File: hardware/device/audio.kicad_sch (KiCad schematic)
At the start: 42 parts, among them J5 AUDIO_EXP, J6 LINE_IN, J7 LINE_OUT, J9 HP_OUT, U24 WM8904CGEFL/RV, U28 TPS560200, U29 MAX98306xDT

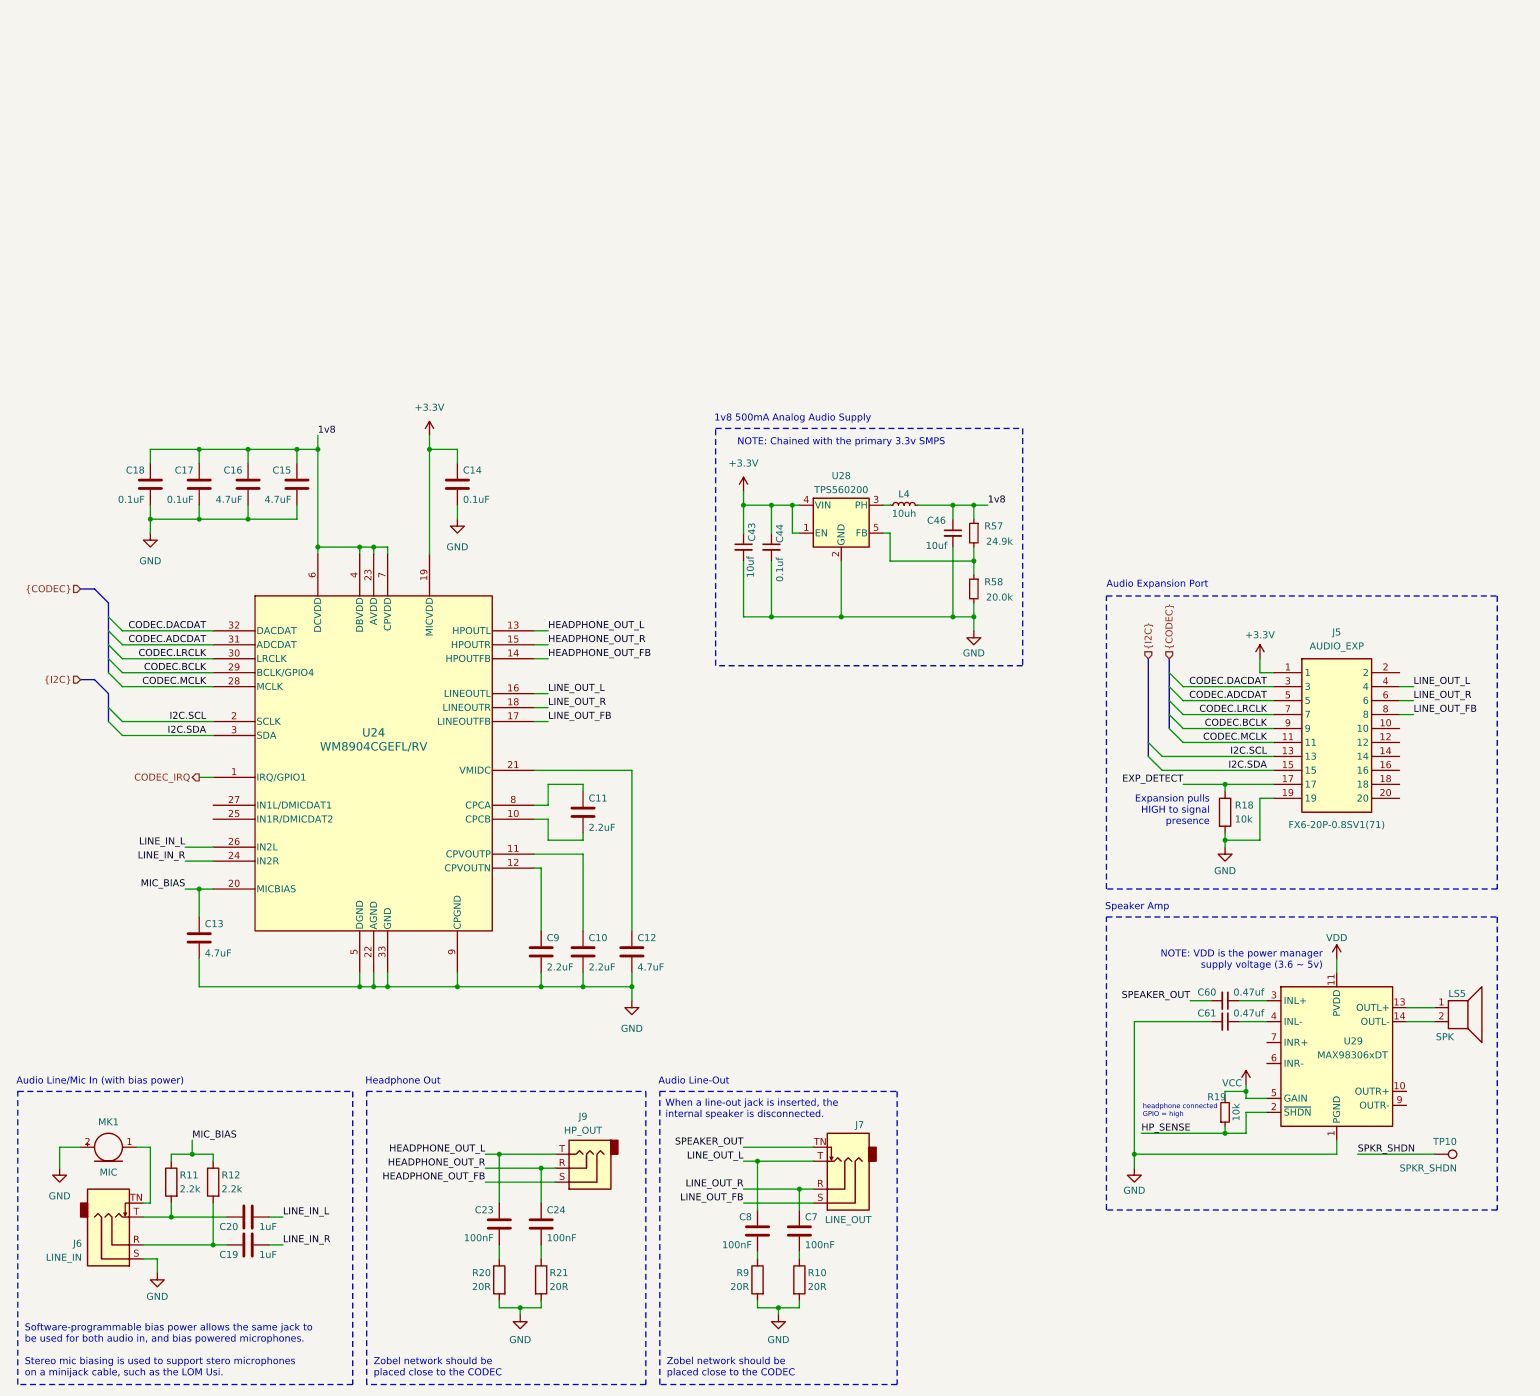
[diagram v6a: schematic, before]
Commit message: feat: change codec to NAU88C22YG
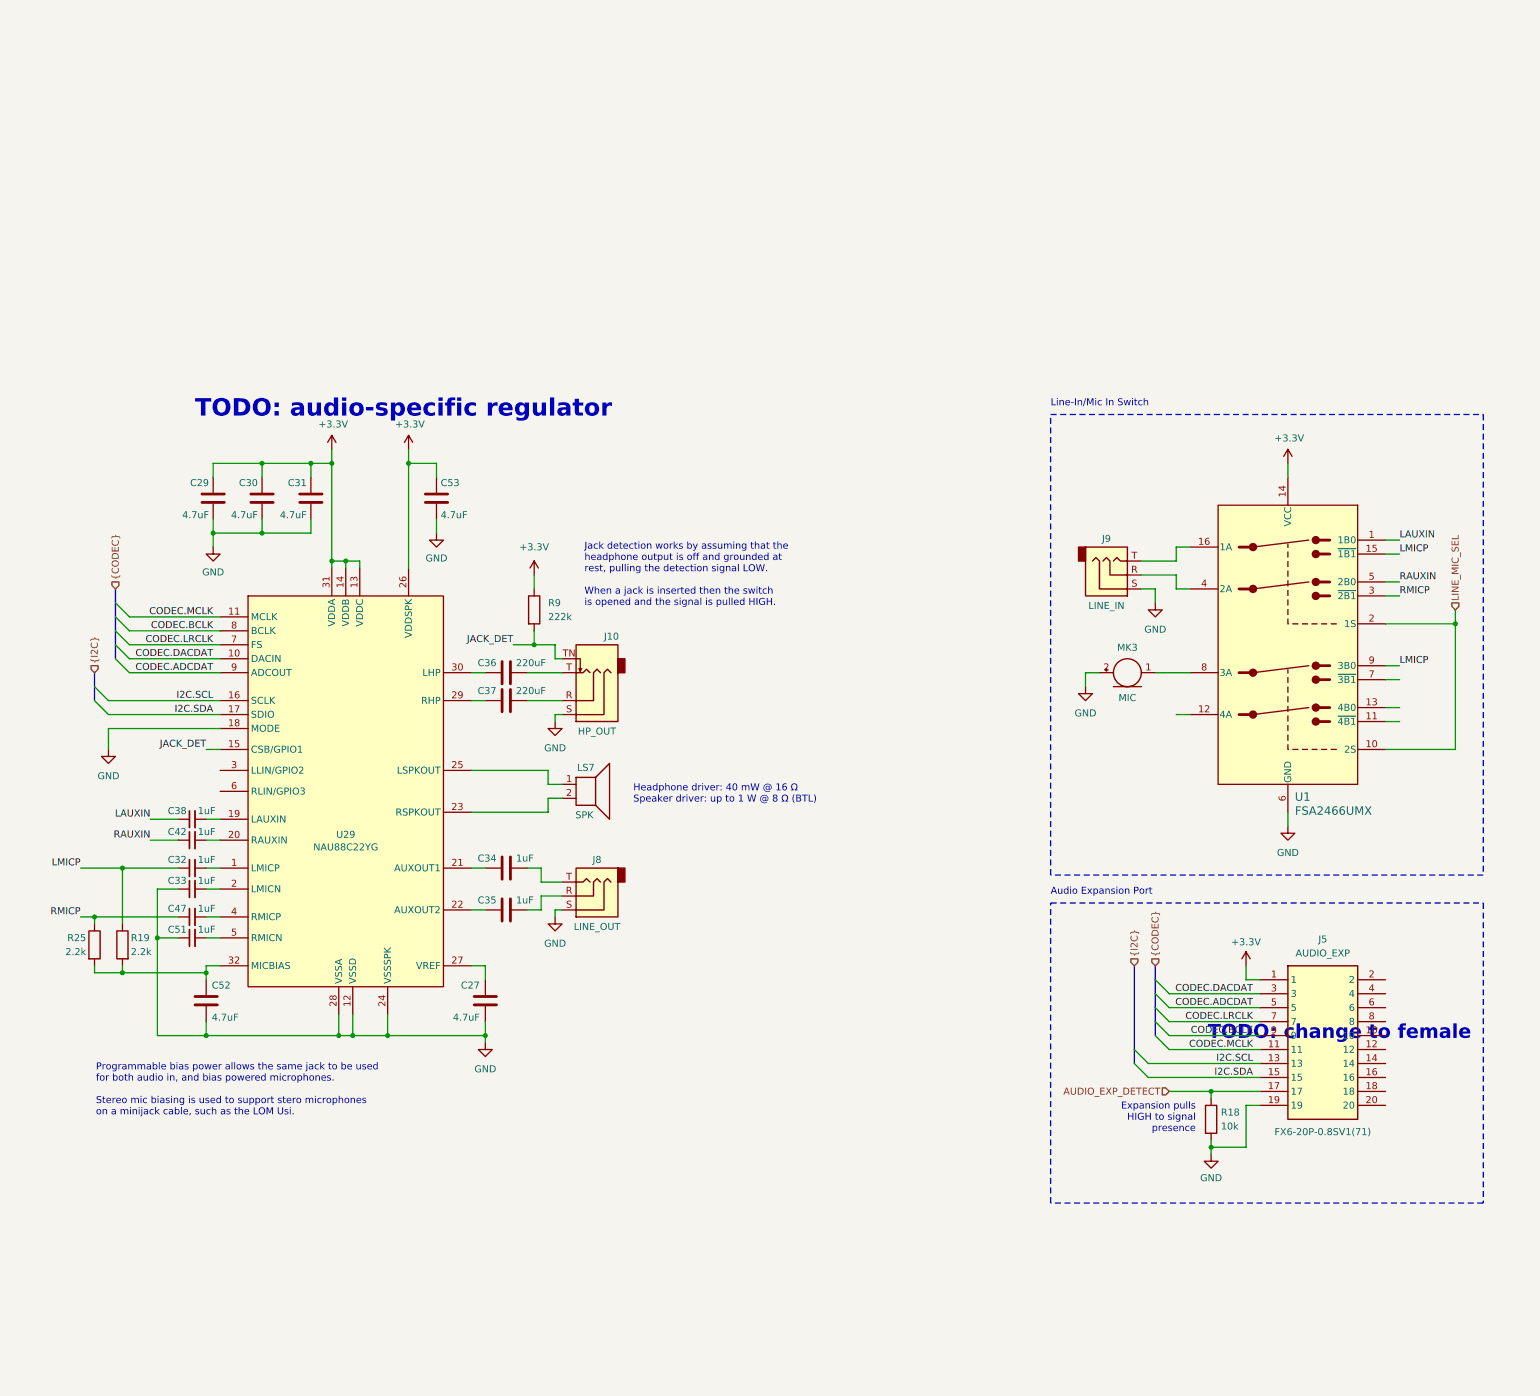
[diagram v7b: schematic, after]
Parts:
- removed C10, C11, C9: 2.2uF, Capacitor_SMD:C_0201_0603Metric, symbol Device:C
- removed C12, C13, C15, C16: 4.7uF, Capacitor_SMD:C_0201_0603Metric, symbol Device:C
- removed C14, C17, C18: 0.1uF, Capacitor_SMD:C_0201_0603Metric, symbol Device:C
- removed C19, C20: 1uF, Capacitor_SMD:C_0201_0603Metric, symbol Device:C
- removed C23, C24, C7, C8: 100nF, Capacitor_SMD:C_0201_0603Metric, symbol Device:C
- removed C43, C46: 10uf, Capacitor_SMD:C_0201_0603Metric, symbol Device:C_Small
- removed C44: 0.1uf, Capacitor_SMD:C_0201_0603Metric, symbol Device:C_Small
- removed C60, C61: 0.47uf, Capacitor_SMD:C_0201_0603Metric, symbol Device:C_Small
- removed J6: LINE_IN, Connector_Audio:Jack_3.5mm_CUI_SJ-3524-SMT_Horizontal, symbol Connector_Audio:AudioJack3_SwitchT
- removed J7: LINE_OUT, Connector_Audio:Jack_3.5mm_CUI_SJ-3524-SMT_Horizontal, symbol Connector_Audio:AudioJack3_SwitchT
- removed L4: 10uh, symbol Device:L_Small
- removed LS5: SPK, symbol Device:Speaker
- removed MK1: MIC, symbol Device:Microphone
- removed R10, R20, R21: 20R, Resistor_SMD:R_0201_0603Metric, symbol Device:R
- removed R11, R12: 2.2k, Resistor_SMD:R_0201_0603Metric, symbol Device:R
- removed R19: 10k, Resistor_SMD:R_0201_0603Metric, symbol Device:R_Small
- removed R57: 24.9k, Resistor_SMD:R_0201_0603Metric, symbol Device:R_Small
- removed R58: 20.0k, Resistor_SMD:R_0201_0603Metric, symbol Device:R_Small
- removed TP10: SPKR_SHDN, TestPoint:TestPoint_Pad_D2.5mm, symbol Connector:TestPoint
- removed U24: WM8904CGEFL/RV, pocket_synth:WM8904CGEFL_RV, symbol pocket_synth:WM8904CGEFL_RV
- removed U28: TPS560200, Package_TO_SOT_SMD:SOT-23-5, symbol Regulator_Switching:TPS560200
- removed U29: MAX98306xDT, Package_DFN_QFN:TDFN-14-1EP_3x3mm_P0.4mm_EP1.78x2.35mm, symbol Amplifier_Audio:MAX98306xDT
- added C27, C29, C30, C31, C52, C53: 4.7uF, Capacitor_SMD:C_0201_0603Metric, symbol Device:C
- added C32, C33, C38, C42, C47, C51: 1uF, Capacitor_SMD:C_0201_0603Metric, symbol Device:C_Small
- added C34, C35: 1uF, Capacitor_SMD:C_0201_0603Metric, symbol Device:C
- added C36, C37: 220uF, Capacitor_SMD:C_0201_0603Metric, symbol Device:C
- added J10: HP_OUT, Connector_Audio:Jack_3.5mm_CUI_SJ-3524-SMT_Horizontal, symbol Connector_Audio:AudioJack3_SwitchT
- added J8: LINE_OUT, Connector_Audio:Jack_3.5mm_CUI_SJ-3523-SMT_Horizontal, symbol Connector_Audio:AudioJack3
- added LS7: SPK, symbol Device:Speaker
- added MK3: MIC, symbol Device:Microphone
- added R19, R25: 2.2k, Resistor_SMD:R_0201_0603Metric, symbol Device:R
- added U1: FSA2466UMX, pocket_synth:FSA2466UMX, symbol pocket_synth:FSA2466UMX
- added U29: NAU88C22YG, pocket_synth:NAU88C22YG, symbol pocket_synth:NAU88C22YG
- J9: value HP_OUT -> LINE_IN
- R9: value 20R -> 222k
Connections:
- net HEADPHONE_OUT_FB is gone; now on net GND: J9.S
- net +3.3V: now also R9.1, C29.1, C30.1, C31.1, C53.1, U1.14 (VCC), U29.13 (VDDC), U29.14 (VDDB), U29.26 (VDDSPK), U29.31 (VDDA)
- net CODEC.ADCDAT: now also U29.9 (ADCOUT)
- net CODEC.BCLK: now also U29.8 (BCLK)
- net CODEC.DACDAT: now also U29.10 (DACIN)
- net CODEC.LRCLK: now also U29.7 (FS)
- net CODEC.MCLK: now also U29.11 (MCLK)
- net GND: now also C27.2, C29.2, C30.2, C31.2, C33.1, C51.1, C52.2, C53.2, J10.S, J8.S, MK3.2 (+), U1.6 (GND), U29.12 (VSSD), U29.18 (MODE), U29.24 (VSSSPK), U29.28 (VSSA); no longer R9.2
- net I2C.SCL: now also U29.16 (SCLK)
- net I2C.SDA: now also U29.17 (SDIO)
- net EXP_DETECT renamed AUDIO_EXP_DETECT
- net HEADPHONE_OUT_L: no longer names the net of J9.T
- net HEADPHONE_OUT_L: now also U1.16 (1A)
- net HEADPHONE_OUT_R: no longer names the net of J9.R
- net HEADPHONE_OUT_R: now also U1.4 (2A)
- net LINE_OUT_FB: no longer names the net of J5.8
- net LINE_OUT_L: no longer names the net of J5.4
- net LINE_OUT_R: no longer names the net of J5.6
- new net: C35.2, J8.R
- new net: C34.2, J8.T
- new net: C38.2, U29.19 (LAUXIN)
- new net: C52.1, R19.2, R25.2, U29.32 (MICBIAS)
- new net: C32.2, U29.1 (LMICP)
- new net: C33.2, U29.2 (LMICN)
- new net: C42.2, U29.20 (RAUXIN)
- new net: C34.1, U29.21 (AUXOUT1)
- new net: C35.1, U29.22 (AUXOUT2)
- new net: LS7.2, U29.23 (RSPKOUT)
- new net: LS7.1, U29.25 (LSPKOUT)
- new net: C27.1, U29.27 (VREF)
- new net: C37.1, U29.29 (RHP)
- new net: C36.1, U29.30 (LHP)
- new net: C47.2, U29.4 (RMICP)
- new net: C51.2, U29.5 (RMICN)
- new net: C37.2, J10.R
- new net: C36.2, J10.T
- new net: MK3.1 (-), U1.8 (3A)
- new net JACK_DET: J10.TN, R9.2, U29.15 (CSB/GPIO1)
- new net LAUXIN: C38.1, U1.1 (1B0)
- new net LINE_MIC_SEL: U1.10 (2S), U1.2 (1S)
- new net LMICP: C32.1, R19.1, U1.15 (~{1B1}), U1.9 (3B0)
- new net RAUXIN: C42.1, U1.5 (2B0)
- new net RMICP: C47.1, R25.1, U1.3 (~{2B1})
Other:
- note added: "Headphone driver: 40 mW @ 16 Ω Speaker driver: up to 1 W @ 8 Ω (BTL)"
- note added: "Jack detection works by assuming that the headphone output is off and grounded at rest, pulling the detection signal LOW. When a jack is inserted then the switch is opened and the signal is pulled HIGH."
- note added: "Line-In/Mic In Switch"
- note added: "Programmable bias power allows the same jack to be used for both audio in, and bias powered microphones. Stereo mic biasing is used to support stero microphones on a minijack cable, such as the LOM Usi."
- note added: "TODO: audio-specific regulator"
- note added: "TODO: change to female"
- note removed: "1v8 500mA Analog Audio Supply"
- note removed: "Audio Line-Out"
- note removed: "Audio Line/Mic In (with bias power)"
- note removed: "Headphone Out"
- note removed: "NOTE: Chained with the primary 3.3v SMPS"
- note removed: "NOTE: VDD is the power manager supply voltage (3.6 ~ 5v)"
- note removed: "Software-programmable bias power allows the same jack to be used for both audio in, and bias powered microphones. Stereo mic biasing is used to support stero microphones on a minijack cable, such as the LOM Usi."
- note removed: "Speaker Amp"
- note removed: "When a line-out jack is inserted, the internal speaker is disconnected."
- note removed: "Zobel network should be placed close to the CODEC"
- note removed: "headphone connected GPIO = high"
- moved on the sheet: J5, R18

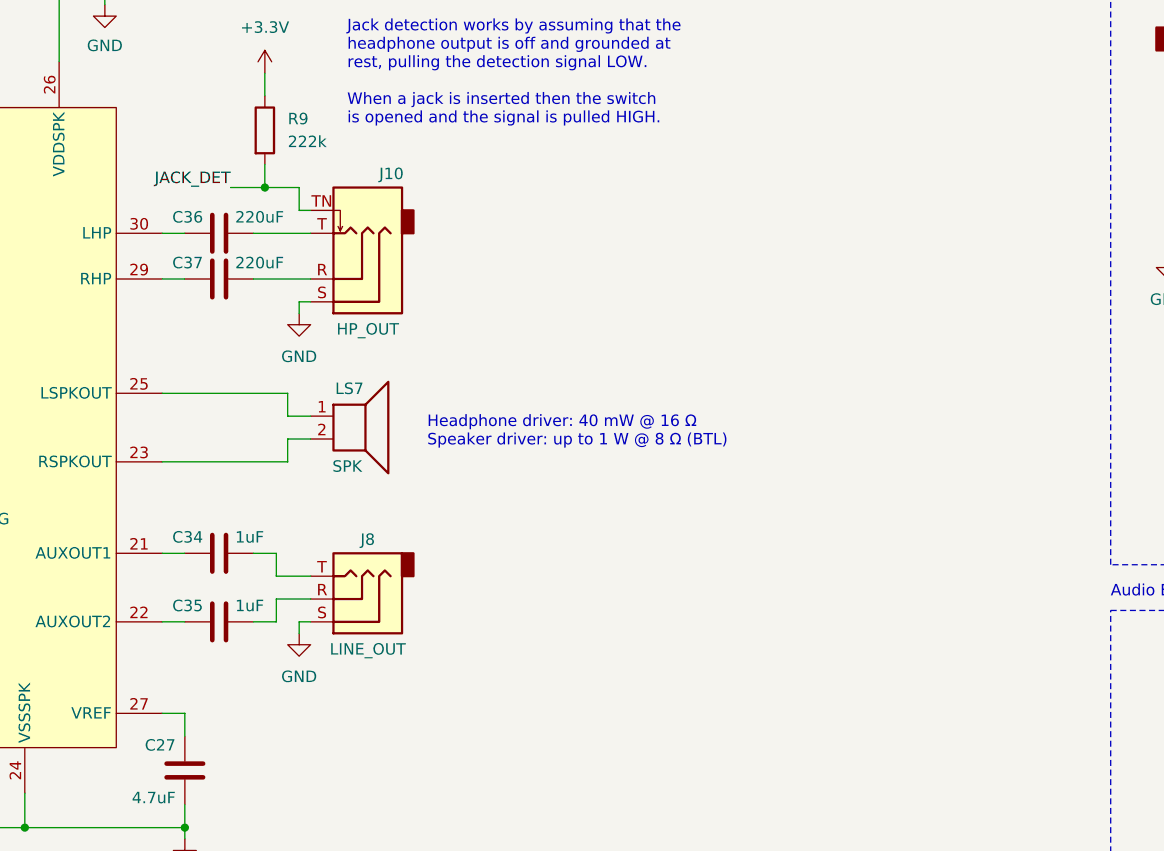
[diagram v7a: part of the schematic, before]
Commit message: feat: add speaker
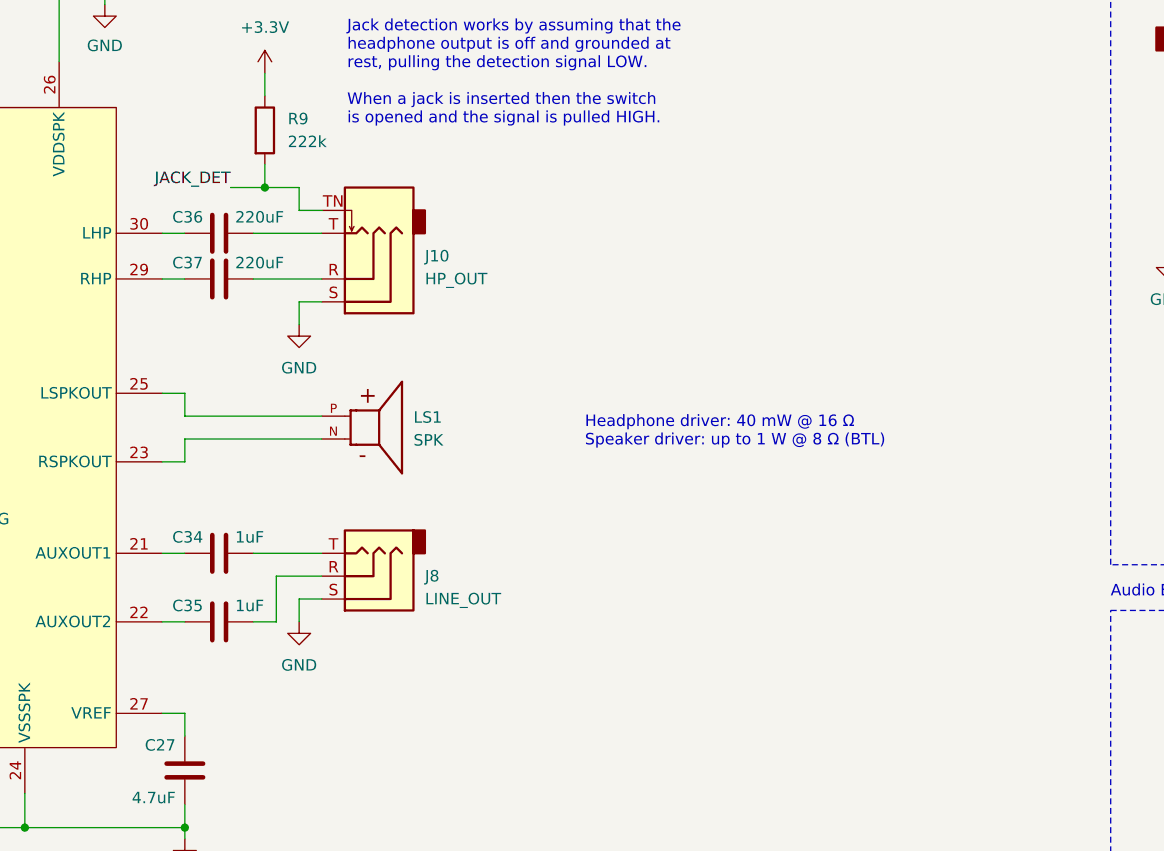
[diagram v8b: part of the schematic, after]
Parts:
- removed LS7: SPK, symbol Device:Speaker
- added LS1: SPK, pocket_synth:AS01808AO-SC18-WP-R, symbol pocket_synth:AS01808AO-SC18-WP-R
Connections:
- net at U29.23 (RSPKOUT): now also LS1.N
- net at U29.25 (LSPKOUT): now also LS1.P
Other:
- moved on the sheet: J10, J8
